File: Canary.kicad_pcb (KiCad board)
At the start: 4 copper layers, 54 x 35 mm, 79 parts, among them J1 CONN_ARM_CM_JTAG_SWD_10, J2 BMD-300-A-R, J3 CONN_20021311-00010T4LF_AMP, J4 USB4125-GF-A, J5 S2B-PH-SM4-TB, Q1 PMN30UNX, Q2 PMN42XPEAH, Q3 PMN30UNX, U1 DNP, U10 MCP73831T-2ATI_OT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

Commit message: Adjust layour
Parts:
- added S1: SM-UART-04L, JetkovKiCADLib:SM-UART-04L, F.Cu at (50.0, 48.5)
- added SW1: TL3301SPF160QG, JetkovKiCADLib:TL3301SPF160QG, B.Cu at (47.5, 67.0)
- moved J5 15.1 mm to (45.3, 52.6), turned to 90 degrees
- moved J1 13.7 mm to (46.6, 56.4)
- moved J4 11.3 mm to (46.5, 67.0)
- moved U2 6.08 mm to (82.5, 75.0)
- moved U6 3.01 mm to (84.8, 59.0)
- moved U3 2.22 mm to (87.8, 74.4)
- moved LS1 2.21 mm to (66.2, 56.4)
- moved J3 1.60 mm to (56.6, 53.9)
- moved J2 0.71 mm to (50.5, 80.5)
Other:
- board size 54 x 35 mm -> 56 x 38 mm

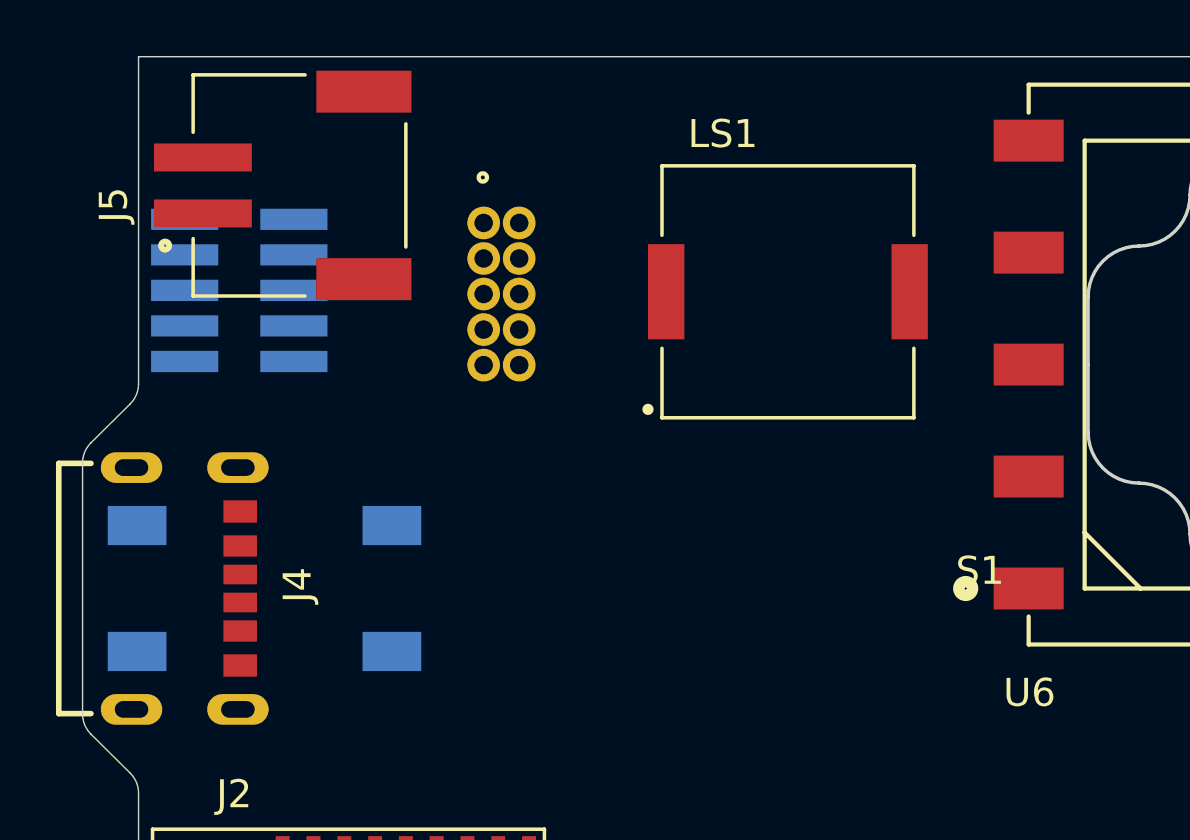
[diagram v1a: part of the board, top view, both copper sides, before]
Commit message: Update switch, placement adjustments
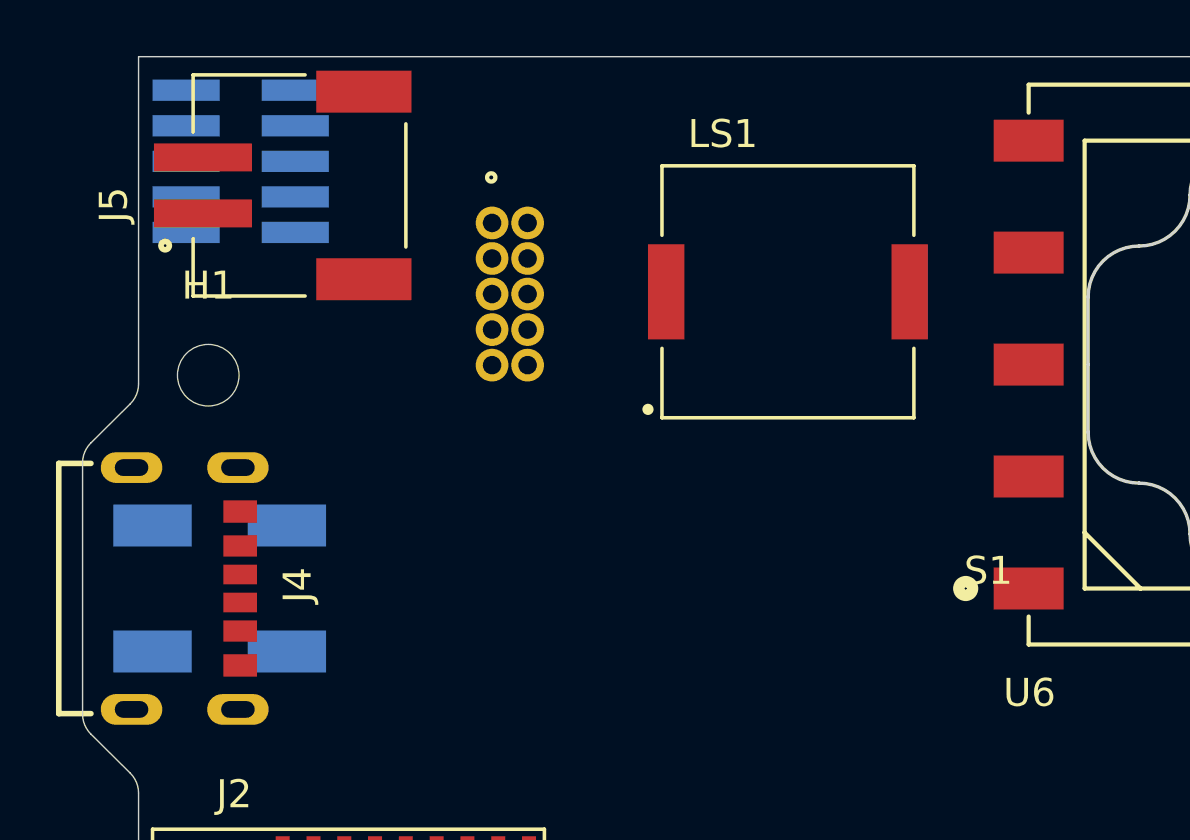
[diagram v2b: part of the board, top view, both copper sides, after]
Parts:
- added H1: MountingHole, Mounting_Holes:MountingHole_2.2mm_M2, F.Cu at (45.5, 59.4)
- J3: value CONN_20021311-00010T4LF_AMP -> 20021311-00010T4LF
- SW1: value TL3301SPF160QG -> TL3301SPF160QJ; footprint JetkovKiCADLib:TL3301SPF160QG -> JetkovKiCADLib:TL3301EF160QJ
- moved J1 4.61 mm to (46.6, 51.7)
- moved SW1 1.60 mm to (45.9, 67.0)
- moved J3 0.30 mm to (56.9, 53.9)
- moved S1 0.30 mm to (50.3, 48.5)
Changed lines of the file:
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@@
     (tracks 0)
     (zones 0)
-    (modules 81)
+    (modules 82)
     (nets 59)
   )
@@
     (add_net ~RESET~)
   )
+  (module JetkovKiCADLib:TL3301EF160QJ (layer B.Cu)
+    (at 45.9 67 180)
+    (fp_text reference SW1 (at 0.4 -4.25) (layer B.SilkS)
+      (effects (font (size 1 1) (thickness 0.15)) (justify mirror))
+    )
+    (fp_text value TL3301SPF160QJ (at 0.55 -6.85) (layer B.Fab) hide
+      (effects (font (size 1 1) (thickness 0.15)) (justify mirror))
+    )
+    (fp_line (start 4.1 -1.2) (end 4.1 -3.3) (layer Dwgs.User) (width 0.12))
+    (fp_line (start 4.1 3.3) (end 4.1 1.2) (layer Dwgs.User) (width 0.12))
+    (fp_line (start 4.1 -1.2) (end 3.5 -1.2) (layer Dwgs.User) (width 0.12))
+    (fp_line (start 3.5 1.2) (end 4.1 1.2) (layer Dwgs.User) (width 0.12))
+    (fp_line (start 3.5 -1.2) (end 3.5 1.2) (layer Dwgs.User) (width 0.12))
+    (fp_line (start -4.1 1.2) (end -4.1 3.3) (layer Dwgs.User) (width 0.12))
+    (fp_line (start -4.1 -3.3) (end -4.1 -1.2) (layer Dwgs.User) (width 0.12))
+    (fp_line (start -3.5 -1.2) (end -4.1 -1.2) (layer Dwgs.User) (width 0.12))
+    (fp_line (start -3.5 1.2) (end -3.5 -1.2) (layer Dwgs.User) (width 0.12))
+    (fp_line (start -4.1 1.2) (end -3.5 1.2) (layer Dwgs.User) (width 0.12))
+    (fp_line (start 4.1 3.3) (end -4.1 3.3) (layer B.CrtYd) (width 0.12))
+    (fp_line (start -4.1 -3.3) (end 4.1 -3.3) (layer B.CrtYd) (width 0.12))
+    (fp_circle (center -4.5 2.258579) (end -4.358579 2.258579) (layer B.SilkS) (width 0.3))
+    (fp_line (start -0.7 -2.3) (end 0.7 -2.3) (layer B.SilkS) (width 0.15))
+    (fp_line (start 0.7 2.3) (end -0.7 2.3) (layer B.SilkS) (width 0.15))
+    (pad 1 smd rect (at -2.4 2.25) (size 2.8 1.5) (layers B.Cu B.Paste B.Mask))
+    (pad 2 smd rect (at 2.4 2.25) (size 2.8 1.5) (layers B.Cu B.Paste B.Mask))
+    (pad 3 smd rect (at -2.4 -2.25 180) (size 2.8 1.5) (layers B.Cu B.Paste B.Mask))
+    (pad 4 smd rect (at 2.4 -2.25 180) (size 2.8 1.5) (layers B.Cu B.Paste B.Mask))
+    (model :JetkovKiCADLib:TL3301SPFxxxxJ.stp
+      (offset (xyz 0 0 0.65))
+      (scale (xyz 1 1 1))
+      (rotate (xyz 0 0 0))
+    )
+  )
+  (module JetkovKiCADLib:JST_S2B-PH-SM4-TB (layer F.Cu)
+    (at 45.3 52.6 90)
+    (attr smd)
+    (fp_text reference J5 (at -0.69228 -3.184 90) (layer F.SilkS)
+      (effects (font (size 1.002189 1.002189) (thickness 0.015)))
+    )
+    (fp_text value S2B-PH-SM4-TB (at 12.17833 9.48143 90) (layer F.Fab)
+      (effects (font (size 1.003575 1.003575) (thickness 0.015)))
+    )
+    (fp_circle (center -2.15 -1.35) (end -2.05 -1.35) (layer F.Fab) (width 0.3))
+    (fp_line (start -3.95 -0.35) (end 3.95 -0.35) (layer F.Fab) (width 0.127))
+    (fp_line (start -3.95 7.25) (end -3.95 -0.35) (layer F.Fab) (width 0.127))
+    (fp_line (start 3.95 7.25) (end -3.95 7.25) (layer F.Fab) (width 0.127))
+    (fp_line (start 3.95 -0.35) (end 3.95 7.25) (layer F.Fab) (width 0.127))
+    (fp_line (start 4.35 -0.6) (end 4.35 7.7) (layer F.CrtYd) (width 0.05))
+    (fp_line (start 1.75 -0.6) (end 4.35 -0.6) (layer F.CrtYd) (width 0.05))
+    (fp_line (start 1.75 -2) (end 1.75 -0.6) (layer F.CrtYd) (width 0.05))
+    (fp_line (start -1.75 -2) (end 1.75 -2) (layer F.CrtYd) (width 0.05))
+    (fp_line (start -1.75 -0.6) (end -1.75 -2) (layer F.CrtYd) (width 0.05))
+    (fp_line (start -4.35 -0.6) (end -1.75 -0.6) (layer F.CrtYd) (width 0.05))
+    (fp_line (start -4.35 7.7) (end -4.35 -0.6) (layer F.CrtYd) (width 0.05))
+    (fp_line (start 4.35 7.7) (end -4.35 7.7) (layer F.CrtYd) (width 0.05))
+    (fp_line (start 3.95 3.65) (end 3.95 -0.35) (layer F.SilkS) (width 0.127))
+    (fp_line (start -2.2 7.25) (end 2.2 7.25) (layer F.SilkS) (width 0.127))
+    (fp_circle (center -2.15 -1.35) (end -2.05 -1.35) (layer F.SilkS) (width 0.3))
+    (fp_line (start -3.95 -0.35) (end -3.95 3.65) (layer F.SilkS) (width 0.127))
+    (fp_line (start -1.9 -0.35) (end -3.95 -0.35) (layer F.SilkS) (width 0.127))
+    (fp_line (start 3.95 -0.35) (end 1.9 -0.35) (layer F.SilkS) (width 0.127))
+    (pad 2 smd rect (at 1 0 90) (size 1 3.5) (layers F.Cu F.Paste F.Mask)
+      (net 2 GND))
+    (pad 1 smd rect (at -1 0 90) (size 1 3.5) (layers F.Cu F.Paste F.Mask)
+      (net 11 +BATT))
+    (pad S1 smd rect (at 3.35 5.75 90) (size 1.5 3.4) (layers F.Cu F.Paste F.Mask)
+      (net 2 GND))
+    (pad S1 smd rect (at -3.35 5.75 90) (size 1.5 3.4) (layers F.Cu F.Paste F.Mask)
+      (net 2 GND))
+    (model :JetkovKiCADLib:S2B-PH-SM4-TB_LF__SN_.step
+      (offset (xyz 0 -7.3 0))
+      (scale (xyz 1 1 1))
+      (rotate (xyz -90 0 0))
+    )
+    (model :JetkovKiCADLib:PHR-2.step
+      (offset (xyz 1 -4 3.2))
+      (scale (xyz 1 1 1))
+      (rotate (xyz -90 0 0))
+    )
+  )
+  (module Mounting_Holes:MountingHole_2.2mm_M2 (layer F.Cu)
+    (at 45.49 59.38)
+    (descr "Mounting Hole 2.2mm, no annular, M2")
+    (tags "mounting hole 2.2mm no annular m2")
+    (attr virtual)
+    (fp_text reference H1 (at 0 -3.2) (layer F.SilkS)
+      (effects (font (size 1 1) (thickness 0.15)))
+    )
+    (fp_text value MountingHole (at 0 3.2) (layer F.Fab)
+      (effects (font (size 1 1) (thickness 0.15)))
+    )
+    (fp_circle (center 0 0) (end 2.45 0) (layer F.CrtYd) (width 0.05))
+    (fp_circle (center 0 0) (end 2.2 0) (layer Cmts.User) (width 0.15))
+    (fp_text user %R (at 0.3 0) (layer F.Fab)
+      (effects (font (size 1 1) (thickness 0.15)))
+    )
+    (pad 1 np_thru_hole circle (at 0 0) (size 2.2 2.2) (drill 2.2) (layers *.Cu *.Mask))
+  )
   (module JetkovKiCADLib:SM-UART-04L locked (layer F.Cu)
-    (at 49.96 48.47)
+    (at 50.26 48.47)
     (attr virtual)
     (fp_text reference S1 (at 23.1 17.9) (layer F.SilkS)
@@
   )
   (module JetkovKiCADLib:20021311-00010T4LF locked (layer B.Cu)
-    (at 56.6 53.94 90)
+    (at 56.9 53.94 90)
     (fp_text reference J3 (at -4.175 2.15 90) (layer B.SilkS)
       (effects (font (size 1 1) (thickness 0.15)) (justify mirror))
     )
-    (fp_text value CONN_20021311-00010T4LF_AMP (at -2.54 -0.635 90) (layer B.SilkS) hide
+    (fp_text value 20021311-00010T4LF (at -2.54 -0.635 90) (layer B.SilkS) hide
       (effects (font (size 1 1) (thickness 0.15)) (justify mirror))
     )
@@
       (scale (xyz 1 1 1))
       (rotate (xyz -90 0 0))
-    )
-  )
-  (module JetkovKiCADLib:TL3301SPF160QG (layer B.Cu)
-    (at 47.5 67 180)
-    (fp_text reference SW1 (at -0.1 -5.9 180) (layer B.SilkS)
-      (effects (font (size 1 1) (thickness 0.15)) (justify mirror))
-    )
-    (fp_text value TL3301SPF160QG (at -0.1 -4.9 180) (layer B.Fab) hide
-      (effects (font (size 1 1) (thickness 0.15)) (justify mirror))
-    )
-    (pad 2 smd rect (at 4.55 -2.25) (size 2.1 1.4) (layers B.Cu B.Paste B.Mask))
-    (pad 3 smd rect (at -4.55 2.25 180) (size 2.1 1.4) (layers B.Cu B.Paste B.Mask))
-    (pad 4 smd rect (at 4.55 2.25) (size 2.1 1.4) (layers B.Cu B.Paste B.Mask))
-    (pad 1 smd rect (at -4.55 -2.25 180) (size 2.1 1.4) (layers B.Cu B.Paste B.Mask))
-    (model :JetkovKiCADLib:TL3301SPFxxxxG.stp
-      (at (xyz 0 0 0))
-      (scale (xyz 1 1 1))
-      (rotate (xyz 0 0 0))
     )
   )
@@
     )
   )
-  (module JetkovKiCADLib:JST_S2B-PH-SM4-TB (layer F.Cu)
-    (at 45.3 52.6 90)
-    (attr smd)
-    (fp_text reference J5 (at -0.69228 -3.184 90) (layer F.SilkS)
-      (effects (font (size 1.002189 1.002189) (thickness 0.015)))
-    )
-    (fp_text value S2B-PH-SM4-TB (at 12.17833 9.48143 90) (layer F.Fab)
-      (effects (font (size 1.003575 1.003575) (thickness 0.015)))
-    )
-    (fp_line (start 3.95 -0.35) (end 1.9 -0.35) (layer F.SilkS) (width 0.127))
-    (fp_line (start -1.9 -0.35) (end -3.95 -0.35) (layer F.SilkS) (width 0.127))
-    (fp_line (start -3.95 -0.35) (end -3.95 3.65) (layer F.SilkS) (width 0.127))
-    (fp_circle (center -2.15 -1.35) (end -2.05 -1.35) (layer F.SilkS) (width 0.3))
-    (fp_line (start -2.2 7.25) (end 2.2 7.25) (layer F.SilkS) (width 0.127))
-    (fp_line (start 3.95 3.65) (end 3.95 -0.35) (layer F.SilkS) (width 0.127))
-    (fp_line (start 4.35 7.7) (end -4.35 7.7) (layer F.CrtYd) (width 0.05))
-    (fp_line (start -4.35 7.7) (end -4.35 -0.6) (layer F.CrtYd) (width 0.05))
-    (fp_line (start -4.35 -0.6) (end -1.75 -0.6) (layer F.CrtYd) (width 0.05))
-    (fp_line (start -1.75 -0.6) (end -1.75 -2) (layer F.CrtYd) (width 0.05))
-    (fp_line (start -1.75 -2) (end 1.75 -2) (layer F.CrtYd) (width 0.05))
-    (fp_line (start 1.75 -2) (end 1.75 -0.6) (layer F.CrtYd) (width 0.05))
-    (fp_line (start 1.75 -0.6) (end 4.35 -0.6) (layer F.CrtYd) (width 0.05))
-    (fp_line (start 4.35 -0.6) (end 4.35 7.7) (layer F.CrtYd) (width 0.05))
-    (fp_line (start 3.95 -0.35) (end 3.95 7.25) (layer F.Fab) (width 0.127))
-    (fp_line (start 3.95 7.25) (end -3.95 7.25) (layer F.Fab) (width 0.127))
-    (fp_line (start -3.95 7.25) (end -3.95 -0.35) (layer F.Fab) (width 0.127))
-    (fp_line (start -3.95 -0.35) (end 3.95 -0.35) (layer F.Fab) (width 0.127))
-    (fp_circle (center -2.15 -1.35) (end -2.05 -1.35) (layer F.Fab) (width 0.3))
-    (pad 2 smd rect (at 1 0 90) (size 1 3.5) (layers F.Cu F.Paste F.Mask)
-      (net 2 GND))
-    (pad 1 smd rect (at -1 0 90) (size 1 3.5) (layers F.Cu F.Paste F.Mask)
-      (net 11 +BATT))
-    (pad S1 smd rect (at 3.35 5.75 90) (size 1.5 3.4) (layers F.Cu F.Paste F.Mask)
-      (net 2 GND))
-    (pad S1 smd rect (at -3.35 5.75 90) (size 1.5 3.4) (layers F.Cu F.Paste F.Mask)
-      (net 2 GND))
-    (model :JetkovKiCADLib:S2B-PH-SM4-TB_LF__SN_.step
-      (offset (xyz 0 -7.3 0))
-      (scale (xyz 1 1 1))
-      (rotate (xyz -90 0 0))
-    )
-  )
   (module JetkovKiCADLib:USB4125-GF-A locked (layer F.Cu)
     (at 46.55 67 270)
@@
   )
   (module JetkovKiCADLib:20021121-00010XXLFc (layer B.Cu)
-    (at 46.6 56.35)
+    (at 46.65 51.74)
     (fp_text reference J1 (at -0.1 4.1) (layer B.SilkS)
       (effects (font (size 0.8 0.8) (thickness 0.015)) (justify mirror))

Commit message: Update switch
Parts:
- moved SW1 0.05 mm to (46.0, 67.0), turned to 0 degrees
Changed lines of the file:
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@@
   )
   (module JetkovKiCADLib:TL3301EF160QJ (layer B.Cu)
-    (at 45.9 67 180)
+    (at 45.95 67)
     (fp_text reference SW1 (at 0.4 -4.25) (layer B.SilkS)
       (effects (font (size 1 1) (thickness 0.15)) (justify mirror))
@@
       (effects (font (size 1 1) (thickness 0.15)) (justify mirror))
     )
+    (fp_line (start 0.7 2.3) (end -0.7 2.3) (layer B.SilkS) (width 0.15))
+    (fp_line (start -0.7 -2.3) (end 0.7 -2.3) (layer B.SilkS) (width 0.15))
+    (fp_circle (center -4.5 2.258579) (end -4.358579 2.258579) (layer B.SilkS) (width 0.3))
+    (fp_line (start -4.1 -3.3) (end 4.1 -3.3) (layer B.CrtYd) (width 0.12))
+    (fp_line (start 4.1 3.3) (end -4.1 3.3) (layer B.CrtYd) (width 0.12))
+    (fp_line (start -4.1 1.2) (end -3.5 1.2) (layer Dwgs.User) (width 0.12))
+    (fp_line (start -3.5 1.2) (end -3.5 -1.2) (layer Dwgs.User) (width 0.12))
+    (fp_line (start -3.5 -1.2) (end -4.1 -1.2) (layer Dwgs.User) (width 0.12))
+    (fp_line (start -4.1 -3.3) (end -4.1 -1.2) (layer Dwgs.User) (width 0.12))
+    (fp_line (start -4.1 1.2) (end -4.1 3.3) (layer Dwgs.User) (width 0.12))
+    (fp_line (start 3.5 -1.2) (end 3.5 1.2) (layer Dwgs.User) (width 0.12))
+    (fp_line (start 3.5 1.2) (end 4.1 1.2) (layer Dwgs.User) (width 0.12))
+    (fp_line (start 4.1 -1.2) (end 3.5 -1.2) (layer Dwgs.User) (width 0.12))
+    (fp_line (start 4.1 3.3) (end 4.1 1.2) (layer Dwgs.User) (width 0.12))
     (fp_line (start 4.1 -1.2) (end 4.1 -3.3) (layer Dwgs.User) (width 0.12))
-    (fp_line (start 4.1 3.3) (end 4.1 1.2) (layer Dwgs.User) (width 0.12))
-    (fp_line (start 4.1 -1.2) (end 3.5 -1.2) (layer Dwgs.User) (width 0.12))
-    (fp_line (start 3.5 1.2) (end 4.1 1.2) (layer Dwgs.User) (width 0.12))
-    (fp_line (start 3.5 -1.2) (end 3.5 1.2) (layer Dwgs.User) (width 0.12))
-    (fp_line (start -4.1 1.2) (end -4.1 3.3) (layer Dwgs.User) (width 0.12))
-    (fp_line (start -4.1 -3.3) (end -4.1 -1.2) (layer Dwgs.User) (width 0.12))
-    (fp_line (start -3.5 -1.2) (end -4.1 -1.2) (layer Dwgs.User) (width 0.12))
-    (fp_line (start -3.5 1.2) (end -3.5 -1.2) (layer Dwgs.User) (width 0.12))
-    (fp_line (start -4.1 1.2) (end -3.5 1.2) (layer Dwgs.User) (width 0.12))
-    (fp_line (start 4.1 3.3) (end -4.1 3.3) (layer B.CrtYd) (width 0.12))
-    (fp_line (start -4.1 -3.3) (end 4.1 -3.3) (layer B.CrtYd) (width 0.12))
-    (fp_circle (center -4.5 2.258579) (end -4.358579 2.258579) (layer B.SilkS) (width 0.3))
-    (fp_line (start -0.7 -2.3) (end 0.7 -2.3) (layer B.SilkS) (width 0.15))
-    (fp_line (start 0.7 2.3) (end -0.7 2.3) (layer B.SilkS) (width 0.15))
-    (pad 1 smd rect (at -2.4 2.25) (size 2.8 1.5) (layers B.Cu B.Paste B.Mask))
-    (pad 2 smd rect (at 2.4 2.25) (size 2.8 1.5) (layers B.Cu B.Paste B.Mask))
-    (pad 3 smd rect (at -2.4 -2.25 180) (size 2.8 1.5) (layers B.Cu B.Paste B.Mask))
-    (pad 4 smd rect (at 2.4 -2.25 180) (size 2.8 1.5) (layers B.Cu B.Paste B.Mask))
+    (pad 4 smd rect (at 2.4 -2.25) (size 2.8 1.5) (layers B.Cu B.Paste B.Mask))
+    (pad 3 smd rect (at -2.4 -2.25) (size 2.8 1.5) (layers B.Cu B.Paste B.Mask))
+    (pad 2 smd rect (at 2.4 2.25 180) (size 2.8 1.5) (layers B.Cu B.Paste B.Mask))
+    (pad 1 smd rect (at -2.4 2.25 180) (size 2.8 1.5) (layers B.Cu B.Paste B.Mask))
     (model :JetkovKiCADLib:TL3301SPFxxxxJ.stp
       (offset (xyz 0 0 0.65))

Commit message: Almost final main component placement
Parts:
- D1, D3: footprint JetkovKiCADLib:LED_0603 -> JetkovKiCADLib:155124xx73200
- D2: value AMBER -> YELLOW; footprint JetkovKiCADLib:LED_0603 -> JetkovKiCADLib:155124xx73200
- J3: value 20021311-00010T4LF -> CONN_20021311-00010T4LF_AMP
- moved D1 135.8 mm to (61.0, 84.5), turned to 180 degrees
- moved D2 126.4 mm to (71.0, 84.5), turned to 180 degrees
- moved D3 122.8 mm to (81.0, 84.5), turned to 180 degrees
- moved U5 80.3 mm to (69.0, 72.5)
- moved J5 49.5 mm to (94.8, 52.5), turned to 270 degrees
- moved U3 19.9 mm to (69.4, 66.7), turned to 270 degrees
- moved U2 19.3 mm to (68.8, 61.4), turned to 270 degrees
- moved LS1 15.4 mm to (56.8, 68.6)
- moved U6 10.0 mm to (84.8, 69.0)
- moved H1 1.34 mm to (46.5, 58.5)
- moved J2 0.50 mm to (50.5, 80.0)

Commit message: Board setup and rules
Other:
- net class Default: clearance 0.2 -> 0.1524; trace_width 0.25 -> 0.1524
- rule trace_clearance: 0.2 -> 0.1524
- rule trace_min: 0.2 -> 0.1524
- rule via_min_size: 0.4 -> 0.6
